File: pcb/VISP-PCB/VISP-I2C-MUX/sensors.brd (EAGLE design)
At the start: 16 x 39.9 mm, 41 parts, among them IC1 BMP388, IC2 BMP388, IC3 BMP388, IC4 BMP388, U1 MIC5225-3.3, U2 TCA9546APWR, U3 24C01ASM, U5 BMP280, U6 BMP280, U7 BMP280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

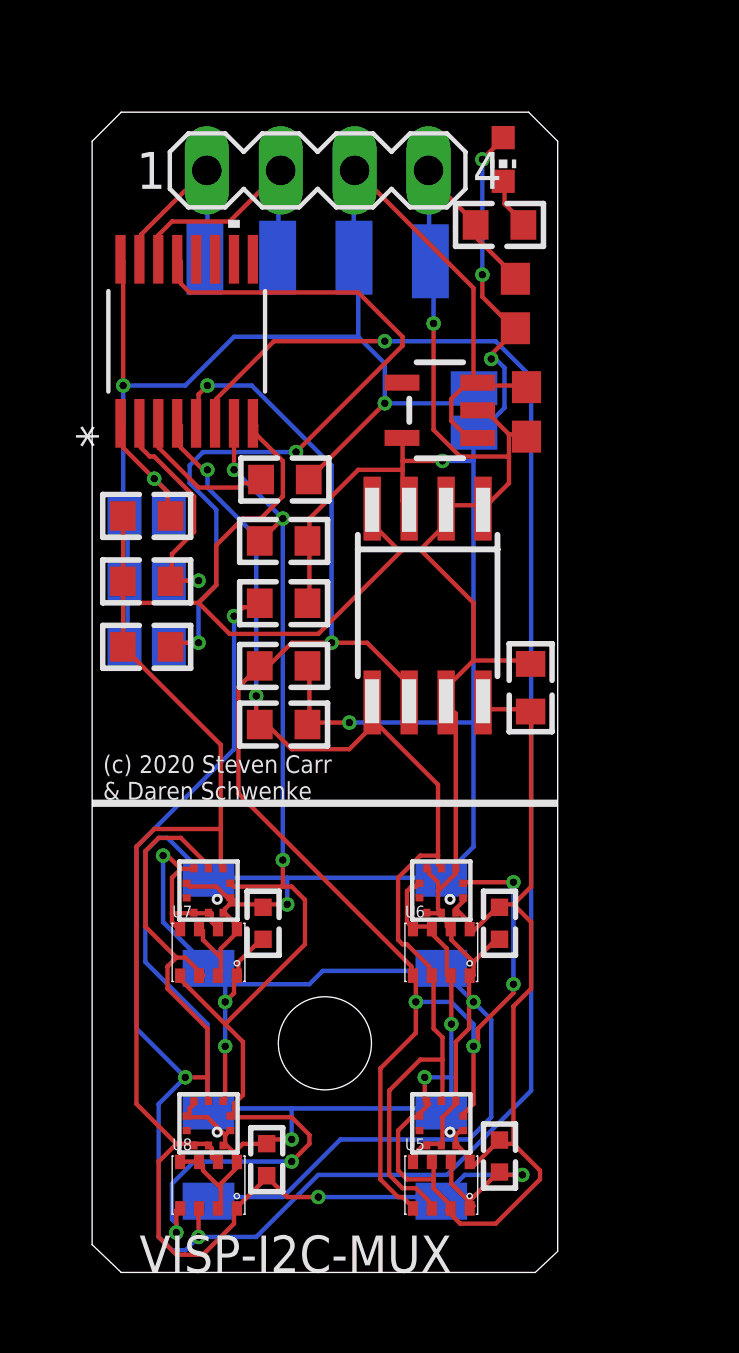
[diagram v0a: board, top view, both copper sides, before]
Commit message: Update I2C MUX board for VISP. Now, it can support a sensor on every pad (for direct comparison analysis) Lowered I2C pullup values.   Each sensor is on it's own I2C bus behind the MUX Wire pads have been brought out to the sides of the OLED pins for somewhat easier wiring
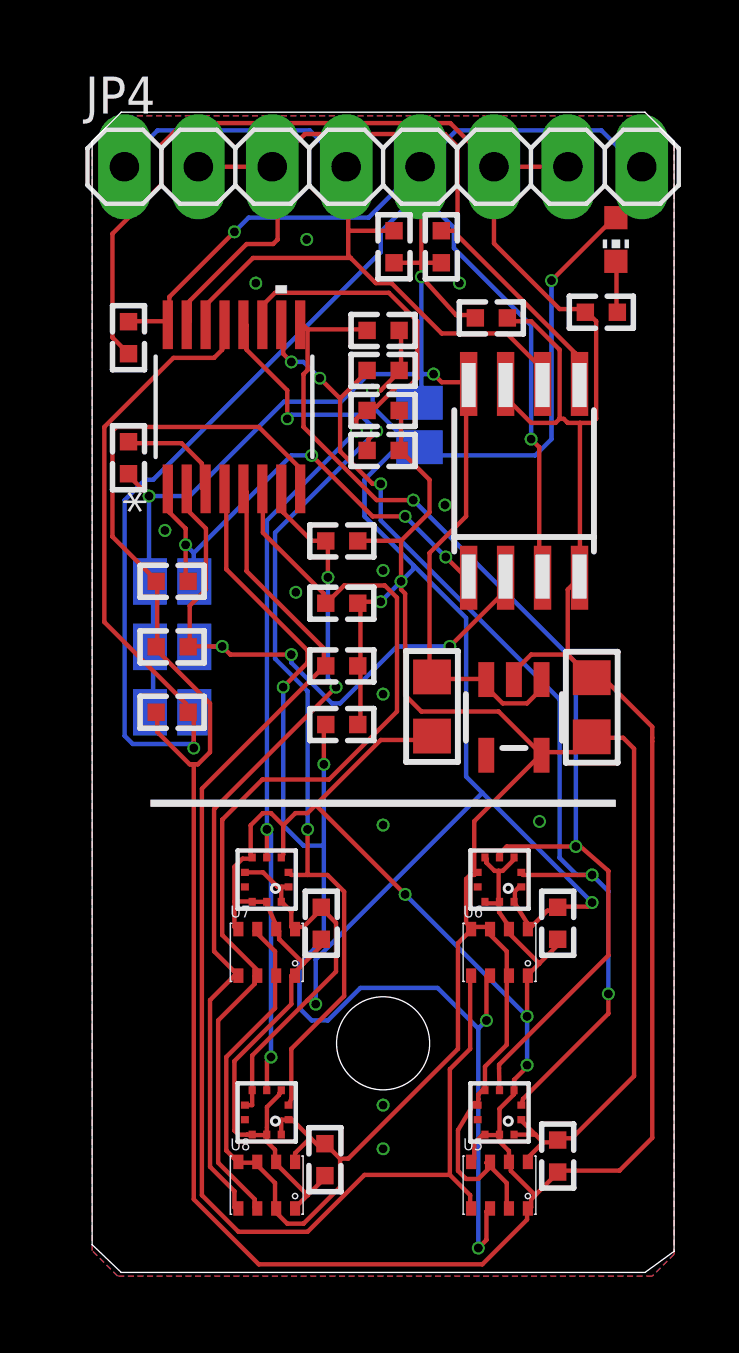
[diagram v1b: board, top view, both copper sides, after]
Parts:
- removed C10, C11, C12, C8: 100nF, Capacitor:CAP1206
- removed GND, SCL, SDA, VCC: (no value), wirepad:SMD1,27-2,54
- removed SV1: (no value), con-lstb:MA04-1
- added C2: 100nF, Capacitor:CAP0402
- added GOLD_ORB_SM1: OSHWLOGOLOGO8MM, oshw:OSHW_8MM
- added JP4: (no value), pinhead-2:1X08
- added R10, R11, R8, R9: 2k7, Resistor:RES0402
- added R12, R13: 4k7, Resistor:RES0402
- C1, C3: device microbuilder:0603-NO -> microbuilder:_0805
- C9: device Capacitor:CAP0603 -> Capacitor:CAP0402
- R1, R2, R22, R23: value 10K Ohms -> 2k7; device Resistor:RES0603 -> Resistor:RES0402
- R3, R4, R5, R6, R7: device Resistor:RES0603 -> Resistor:RES0402
- moved C3 14.1 mm to (17.2, 19.4)
- moved C9 12.8 mm to (13.7, 32.8), turned to 0 degrees
- moved U1 10.9 mm to (14.5, 19.1), turned to 180 degrees
- moved C1 10.6 mm to (11.7, 19.4)
- moved R7 5.43 mm to (1.25, 28.0), turned to 270 degrees
- moved U3 5.42 mm to (14.8, 27.2), turned to 0 degrees
- moved LED1 4.75 mm to (18.0, 35.5)
- moved R4 4.61 mm to (17.5, 33.0)
- moved U2 2.78 mm to (4.88, 29.8)
- moved R3 2.41 mm to (2.75, 23.8)
- moved R5 2.41 mm to (2.75, 21.5)
- moved R6 2.41 mm to (2.75, 19.2)
- moved SJ1 2.41 mm to (2.75, 23.8)
- moved SJ2 2.41 mm to (2.75, 21.5)
- moved SJ3 2.41 mm to (2.75, 19.2)
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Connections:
- new net SCK3_3V: IC3.2, IC4.2, R10.1, U2.10
- new net SCK4_3V: IC1.2, IC2.2, R11.1, U2.12
- new net SDI3_3V: IC3.4, IC4.4, R8.1, U2.9
- new net SDI4_3V: IC1.4, IC2.4, R9.1, U2.11
- net 3.3V: now also R10.2, R11.2, R8.2, R9.2; no longer C10.1, C11.1, C12.1, C8.1, C9.1, U3.3, U3.8
- net 5.0V: now also C2.1, C9.1, JP4.5, JP4.8, R12.2, R13.2, U3.8; no longer SV1.3, VCC.1
- net A0: now also U3.1
- net A1: now also U3.2
- net A2: now also U3.3
- net GND: now also C2.2, JP4.6, JP4.7; no longer C10.2, C11.2, C12.2, C8.2, GND.1, SV1.4, U3.1, U3.2
- net SCK1_3V: no longer IC3.2, IC4.2, U3.6
- net SCK2_3V: no longer IC1.2, IC2.2
- net SCL_5V: now also JP4.1, JP4.4, R13.1, U3.6; no longer SCL.1, SV1.2
- net SDA_5V: now also JP4.2, JP4.3, R12.1, U3.5; no longer SDA.1, SV1.1
- net SDI1_3V: no longer IC3.4, IC4.4, U3.5
- net SDI2_3V: no longer IC1.4, IC2.4
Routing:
- net SDI2_3V: track 93.3 -> 34.2 mm, vias 4 -> 0
- net SDI3_3V: track 0.00 -> 38.2 mm, vias 0 -> 2
- net SCK3_3V: track 0.00 -> 37.3 mm, vias 0 -> 5
- net SDI4_3V: track 0.00 -> 36.7 mm, vias 0 -> 3
- net SCK4_3V: track 0.00 -> 35.5 mm, vias 0 -> 3
- net A2: track 27.5 -> 59.7 mm
- net 3.3V: track 144.1 -> 165.1 mm, vias 9 -> 6
- net SDA_5V: track 7.10 -> 27.4 mm
- net SCL_5V: track 9.00 -> 28.6 mm
- net 5.0V: track 51.7 -> 71.1 mm, vias 2 -> 4
- net GND: track 172.0 -> 188.0 mm, vias 7 -> 15
- net SCK2_3V: track 43.0 -> 28.8 mm, vias 5 -> 2
- net A1: track 8.58 -> 20.8 mm, vias 1 -> 3
- net A0: track 5.40 -> 17.4 mm, vias 1 -> 4
- net SCK1_3V: track 55.7 -> 45.7 mm, vias 6 -> 0
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- added copper zone on layer 1, net GND
- added copper zone on layer 16, net GND
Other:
- board size 16 x 39.9 mm -> 20 x 39.9 mm
- board text added: "ADDR[012] Selection open | closed = chip I2C Addr 0x70 + [ADDR] = TCA9546 0x50 + [ADDR] = EEPROM Bus 1 0x76 = U7 0x77 = U8 Bus 2 (pitot) 0x76 = U5 0x77 = U6 (c) 2020 Steven Carr & Daren Schwenke"
- board text added: "GND"
- board text added: "SCL"
- board text added: "SDA"
- board text added: "VCC"
- board text added: "Vreg Bypass"
- board text removed: "(c) 2020 Steven Carr & Daren Schwenke"
- board text removed: "ADDR Selection open | closed = chip I2C Addr 0x70 | 0x71 Mux Addr Bus 1 0x50 = EEPROM 0x76 = U7 0x77 = U8 Bus 2 0x76 = U5 0x77 = U6 (c) 2020 Steven Carr & Daren Schwenke"
- board text removed: "U3 Bypass"

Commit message: Update VISP-I2C-MUX for manufacturing by OSH-Park All 8 sensor pads can be populated simultaneously without I2C bus conflicts. Updated board text to reflect new capabilities Increased width slightly to satisfy OSH-parks 2-Layer rules.
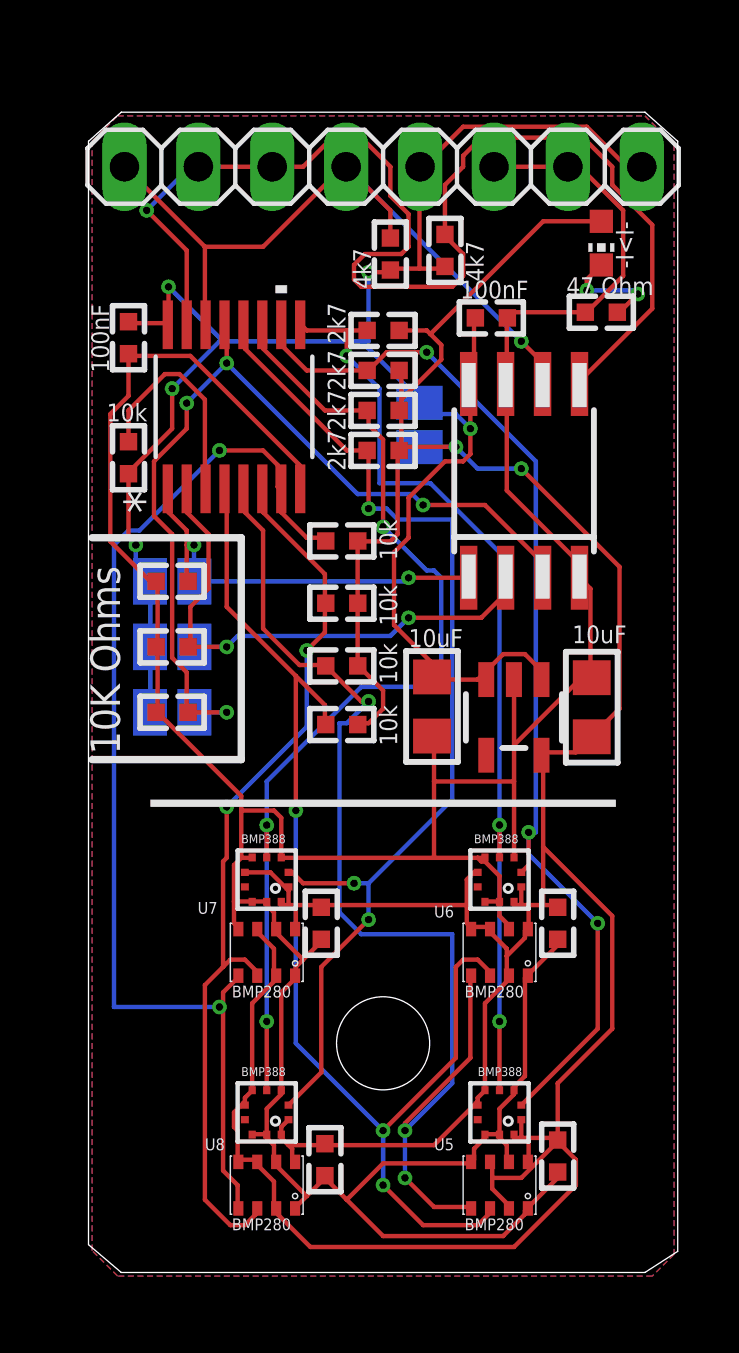
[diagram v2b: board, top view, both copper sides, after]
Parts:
- moved LED1 0.52 mm to (17.5, 35.4)
- moved R13 0.28 mm to (10.2, 35.0)
- moved R12 0.18 mm to (12.1, 35.1)
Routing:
- net GND: track 188.0 -> 128.0 mm, vias 15 -> 0
- net 3.3V: track 165.1 -> 128.1 mm, vias 6 -> 2
- net A2: track 59.7 -> 31.6 mm, vias 2 -> 4
- net SDA_5V: track 27.4 -> 43.5 mm, vias 0 -> 1
- net SCK2_3V: track 28.8 -> 38.9 mm
- net SCK1_3V: track 45.7 -> 39.8 mm, vias 0 -> 3
- net SDI3_3V: track 38.2 -> 32.8 mm, vias 2 -> 3
- net 5.0V: track 71.1 -> 67.2 mm, vias 4 -> 5
- net RESET: track 3.83 -> 7.65 mm
- net SDI2_3V: track 34.2 -> 31.2 mm, vias 0 -> 2
- net A0: track 17.4 -> 14.5 mm, vias 4 -> 2
- net SCL_5V: track 28.6 -> 26.0 mm, vias 0 -> 1
- net SDI1_3V: track 43.4 -> 41.2 mm, vias 4 -> 3
- net LED: track 1.76 -> 3.84 mm, vias 0 -> 2
- net SDI4_3V: track 36.7 -> 35.1 mm
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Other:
- board size 20 x 39.9 mm -> 20.2 x 39.9 mm
- board text added: "ADDR[012] Selection open | closed = chip I2C Addr 0x70 + [ADDR] = TCA9546 0x50 + [ADDR] = EEPROM Bus 1 (BMP280) 0x76 = U7 0x77 = U8 Bus 2 (pitot, BMP280) 0x76 = U5 0x77 = U6 Bus 3 (BMP388) 0x76 = U7 0x77 = U8 Bus 4 (pitot, BMP388) 0x76 = U5 0x77 = U6 (c) 2020 Steven Carr & Daren Schwenke"
- board text added: "BMP388"
- board text removed: "ADDR[012] Selection open | closed = chip I2C Addr 0x70 + [ADDR] = TCA9546 0x50 + [ADDR] = EEPROM Bus 1 0x76 = U7 0x77 = U8 Bus 2 (pitot) 0x76 = U5 0x77 = U6 (c) 2020 Steven Carr & Daren Schwenke"
